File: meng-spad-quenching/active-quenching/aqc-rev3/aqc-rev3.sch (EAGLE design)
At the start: 252 parts, among them IC1 TPS7A4901, IC10 TPS7A3001, IC11 LT1534-1, IC12 74AHC1G04DBV, IC13 TLV271DBV, IC14 NC7WZ16P6X, IC15 LTC1711, IC16 HFA3134, IC17 HFA3135, IC18 USBLC6-2SC6Y, IC19 HFA3135, IC2 TPS7A4901, IC20 HFA3134, IC21 STM32F411RE, IC22 MAX572X, IC23 HFA3134, IC24 LM1117, IC25 HFA3134, IC26 THAT320, IC3 LT1534-1, IC4 TLV272DGK, IC5 ADCMP582, IC6 DS1100LU-20+, IC7 HFA3134, IC8 NC7SV74K8X, IC9 HFA3134, M1 BSS806N, M2 BSS806N, M3 BSS806N, Q6 IRLML6402TRPBF, SW1 MCU_RST, U1 MCP4725, U2 SN65EPT22DGK, U3 SN65EPT21DGK, X1 CONN_PULLDN_SENSE, X2 CONN_FORCE_QUENCH, X3 KEYSTONE-7774, X4 CONN_SPAD, X5 CONN_PHOTON_COUNTER, X6 KEYSTONE-7774, X7 CONN_SMU, X8 PN61729-S

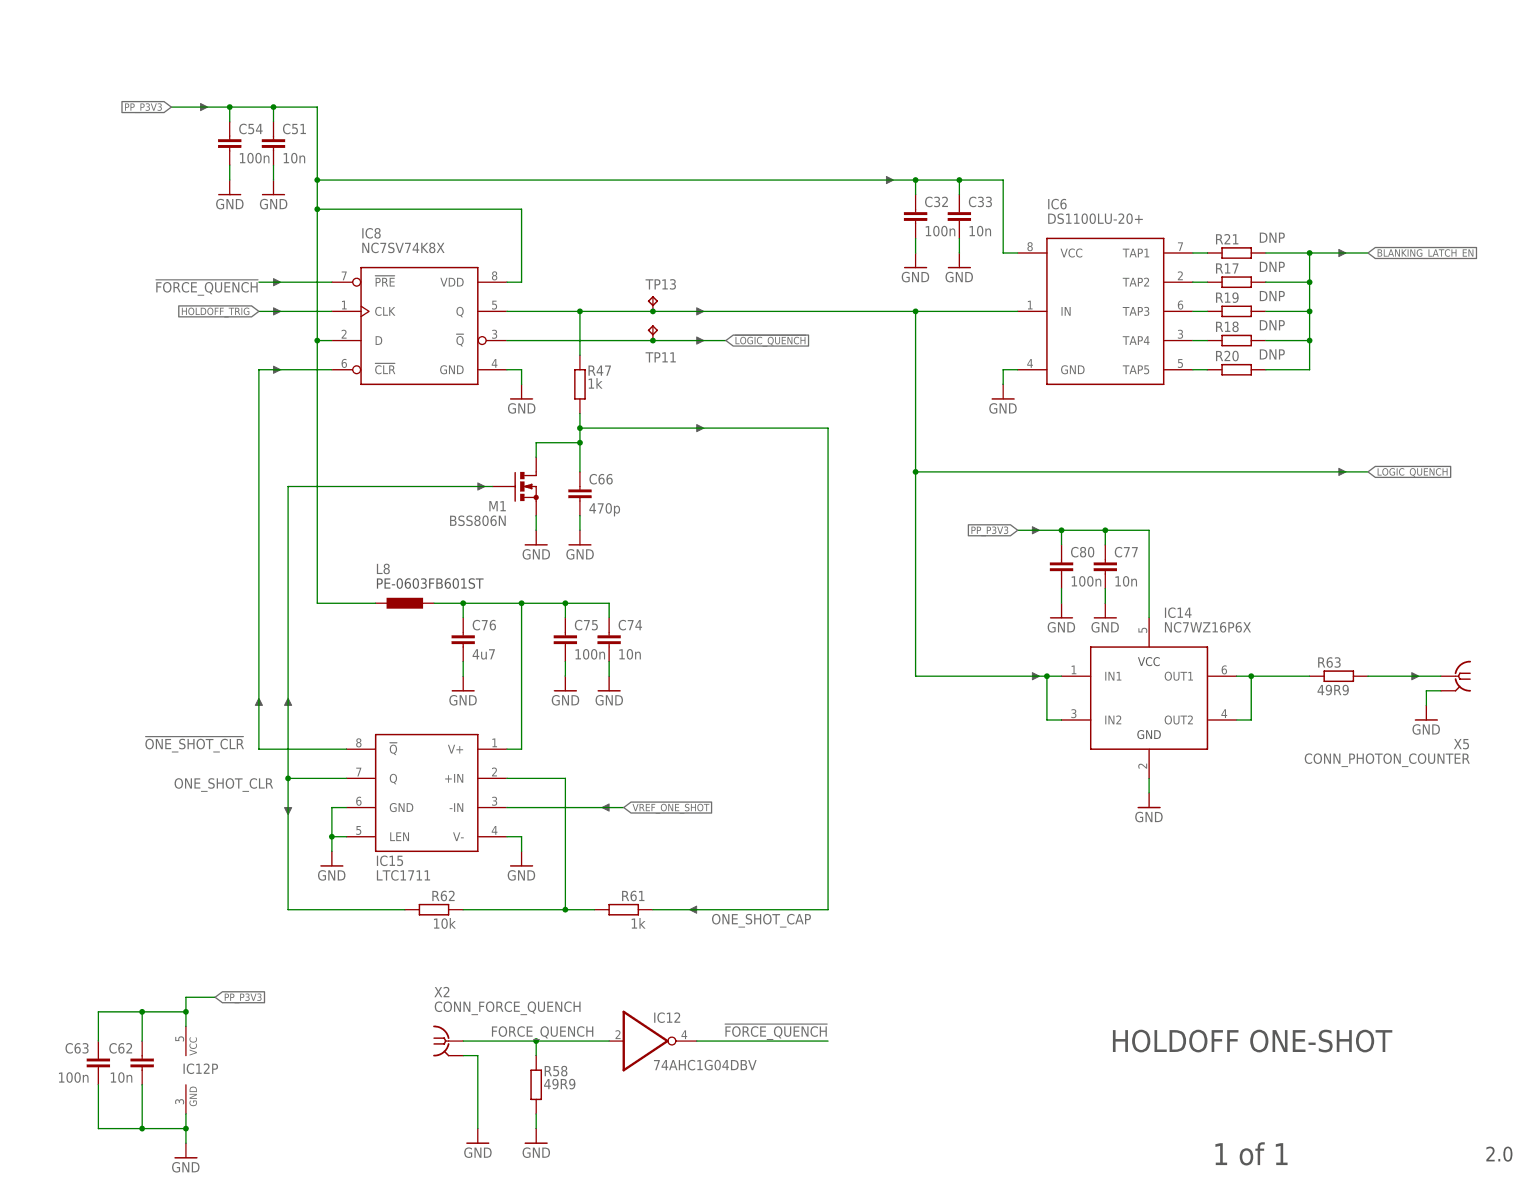
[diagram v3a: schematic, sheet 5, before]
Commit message: Improvements to one-shot and logic, more layout
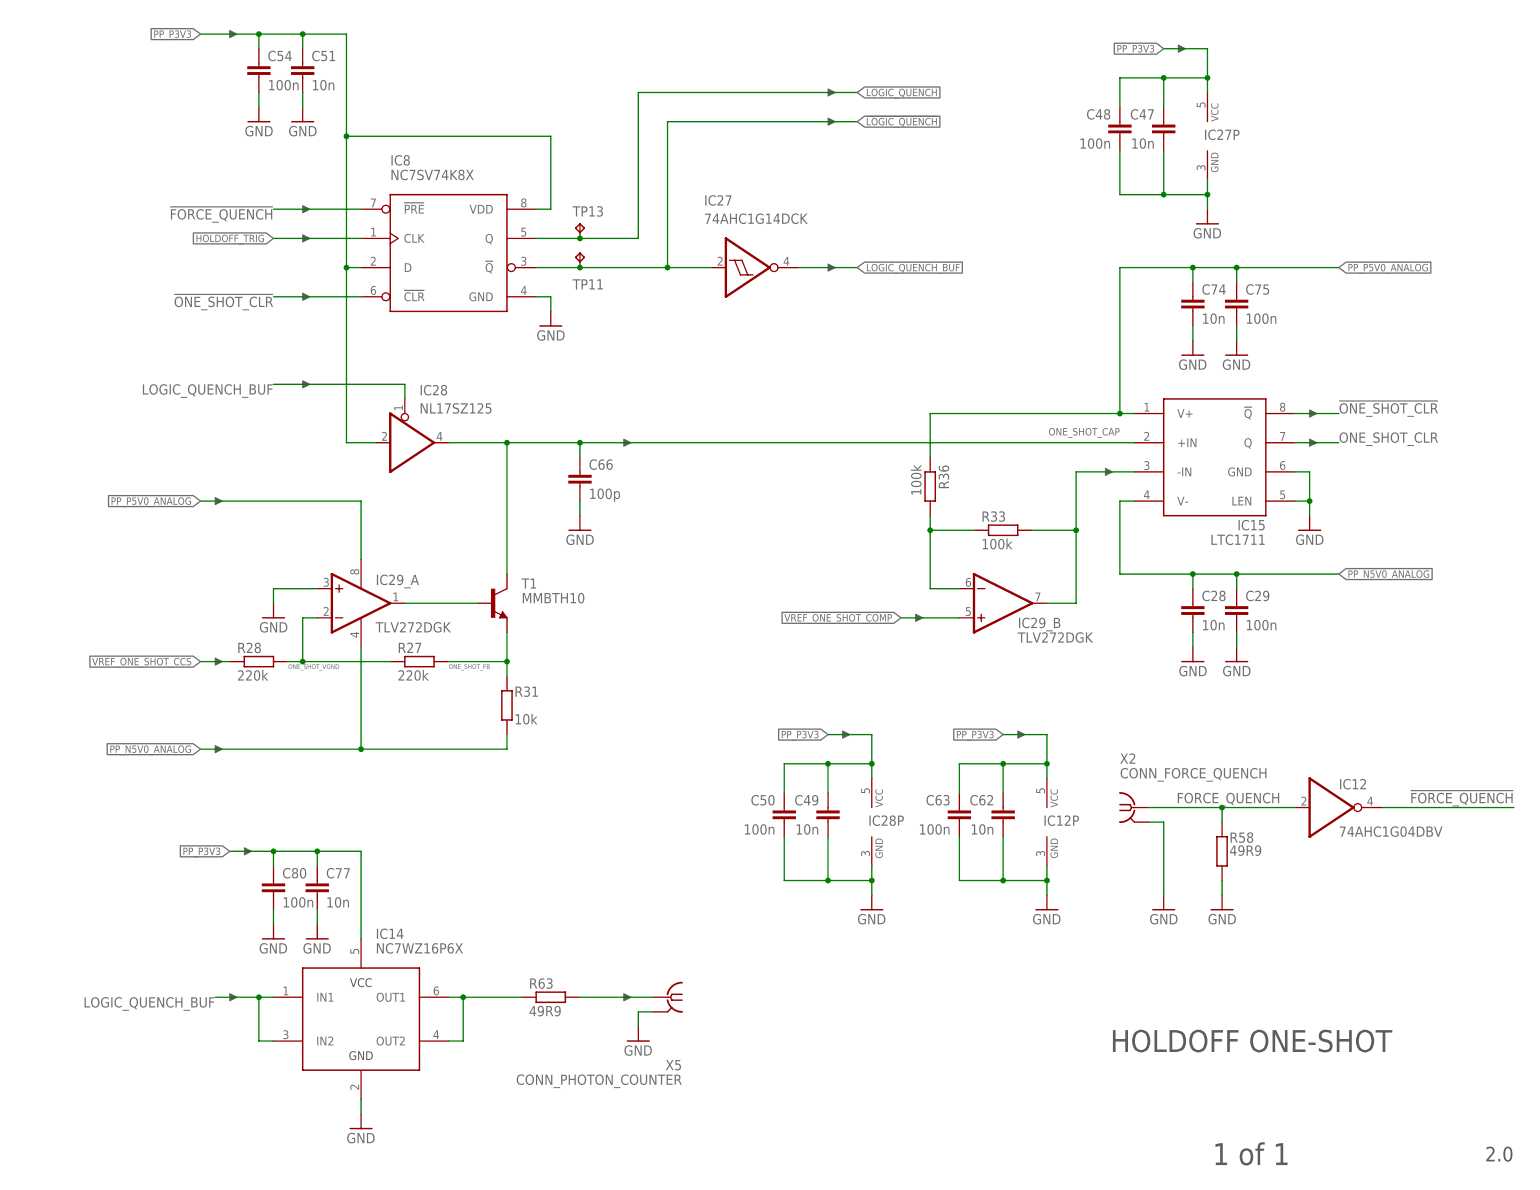
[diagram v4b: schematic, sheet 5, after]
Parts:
- removed C55: 100n, rcl-modified-footprints:C-EUC0603
- removed C76: 4u7, rcl:C-EUC0603
- removed L8: PE-0603FB601ST, meng:INDUCTOR0603
- removed M1: BSS806N, meng:BSS806N
- removed R47, R61: 1k, rcl:R-EU_R0603
- removed R62: 10k, rcl:R-EU_R0603
- added C19, C20, C28, C47, C49: 10n, rcl-modified-footprints:C-EUC0402
- added C29, C43, C48, C50: 100n, rcl-modified-footprints:C-EUC0402
- added IC27: 74AHC1G14DCK, 74xx-little-de:74AHC1G14DCK
- added IC28: NL17SZ125, 74xx-little-de:74AHC1G125DCK
- added IC29: TLV272DGK, meng:TLV272DGK
- added R27, R28: 220k, rcl-modified-footprints:R-EU_R0603
- added R31: 10k, rcl-modified-footprints:R-EU_R0603
- added R33, R36: 100k, rcl-modified-footprints:R-EU_R0603
- added R37, R42: DNP, rcl-modified-footprints:R-EU_R0603
- added T1: MMBTH10, transistor:MMBTH10LT1-NPN-SOT23-BEC
- C21: value 10n -> 100n
- C22, C27, C35, C42, C74, C75: device rcl:C-EUC0402 -> rcl-modified-footprints:C-EUC0402
- C36: value 1n -> 10n
- C37: value 100n -> 10n
- C66: value 470p -> 100p; device rcl:C-EUC0603 -> rcl-modified-footprints:C-EUC0603
- C95, C96: device rcl:C-EUC0603 -> rcl-modified-footprints:C-EUC0603
- R14: value 100R -> 1k
- R65: device rcl:R-EU_R0603 -> rcl-modified-footprints:R-EU_R0603
- R73, R81: value 100k -> 220k; device rcl:R-EU_R0603 -> rcl-modified-footprints:R-EU_R0603
- TP14: value CASC_IBIAS -> DELTA_V
- TP17: value SLEW_UP -> V_A
- TP18: value SLEW_DN -> EXTRA_1
- TP19: value SLEW_MAX -> EXTRA_2
- TP20: value (DELAY_UP) -> EXTRA_3
- TP21: value (DELAY_DN) -> EXTRA_4
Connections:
- net N$28 renamed PULLDN_SENSE_R_CONN
- removed net COMP_VP: C36.1, IC5.VP, R14.1
- removed net N$25: IC15.+IN, R61.1, R62.2
- removed net PP_P3V3_COMP: C74.1, C75.1, C76.1, IC15.V+, L8.P$2
- removed net PP_P3V3_DAC2: C17.1, C18.1, L2.P$2, U1.VDD
- removed net VREF_EXTRA_1: IC22.OUT4, TP18.P$1
- removed net VREF_ONE_SHOT: IC15.-IN, IC22.OUT2, TP16.P$1
- new net LOGIC_QUENCH_BUF: IC14.IN1, IC14.IN2, IC27A.O, IC28A.OE, IC6.IN
- new net N$1: R14.2, U1.VOUT
- new net N$10: IC29_B.-IN, R33.2, R36.1
- new net N$5: IC29_A.OUT, T1.B
- new net N$7: IC15.-IN, IC29_B.OUT, R33.1
- new net ONE_SHOT_FB: R27.1, R31.1, T1.E
- new net ONE_SHOT_VGND: IC29_A.-IN, R27.2, R28.1
- new net PP_P3V3_AV_DET_DAC: C17.1, C18.1, L2.P$2, R42.2, U1.VDD
- new net VREF_ONE_SHOT_CCS: IC22.OUT4, R28.2, TP18.P$1
- new net VREF_ONE_SHOT_COMP: IC22.OUT2, IC29_B.+IN, TP16.P$1
- net !LOGIC_QUENCH: now also IC27A.I
- net GND: now also C19.2, C20.2, C28.2, C29.2, C43.2, C47.2, C48.2, C49.2, C50.2, IC27P.GND, IC28P.GND, IC29_A.+IN, R37.1; no longer C55.2, C76.2, IC15.V-, M1.S
- net LOGIC_QUENCH: no longer IC14.IN1, IC14.IN2, IC6.IN, R47.2
- net ONE_SHOT_CAP: now also IC15.+IN, IC28A.O, T1.C; no longer M1.D, R47.1, R61.2
- net ONE_SHOT_CLR: no longer M1.G, R62.1
- net PP_N5V0_ANALOG: now also C28.1, C29.1, IC15.V-, IC29_A.V-, R31.2
- net PP_P15V0_ANALOG: no longer C55.1
- net PP_P3V3: now also C47.1, C48.1, C49.1, C50.1, IC27P.VCC, IC28A.I, IC28P.VCC; no longer L8.P$1
- net PP_P5V0_ANALOG: now also C19.1, C20.1, C74.1, C75.1, IC15.V+, IC29_A.V+, R36.2
- net VREF_AV_DET: now also C36.1, C43.1, IC5.VP, R14.1, R37.2, R42.1; no longer R14.2, U1.VOUT
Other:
- note added: "-IN"
- note added: "5V"
- note added: "Active-Low for Latch Mode (Note how Q0 goes to !LE!)"
- note added: "HIGH = Latch Enabled LOW = Latch Disabled"
- note added: "Insufficient recovery blanking results in self re-triggering Pick lowest delay tap that compensates a given coax cable"
- note added: "Note: comparator input pin has external capacitance connected, keep the driving pt. resistance high enough to ensure DAC opamp stability!"
- note added: "ONE_SHOT_CAP"
- note added: "Quenching can be forced at any time either by uC or from external input"
- note added: "Reduce loading of d-flop as much as possible for fast quenching"
- note added: "Reset holdoff timing cap when not quenching"
- note added: "This CCS BJT is always in FAR"
- note added: "avalanche detected"
- note added: "comp triggered"
- note added: "holdoff time"
- note removed: "4ns per tap, pick lowest tap that provides sufficient recovery blanking"
- note removed: "Active-Low for Latch Mode"
- note removed: "Assert before probe has landed"
- note removed: "From control logic"
- note removed: "HIGH = Latch Enabled"
- note removed: "LOW = Latch Disabled"
- note removed: "Note: insufficient recovery blanking = SPAD voltage oscillation"
- note removed: "Reduce loading of d-flop as much as possible"
- moved on the sheet: C21, C22, C23, C27, C34, C35, C36, C37, C38, C39, C42, C51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

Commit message: work on layout
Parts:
- added C55, C76: 10n, rcl:C-EUC0402
- added C64, C65, C73, C83: 100n, rcl:C-EUC0402
- added IC30: 74AHC1G32DCK, 74xx-little-de:74AHC1G32DCK
- added IC31: 74AHC1G08DCK, 74xx-little-de:74AHC1G08DCK
- added R44: 49R9, rcl:R-EU_R0603
- IC12: value 74AHC1G04DBV -> 74AHC1G04DCK; device 74xx-little-de:74AHC1G04DBV -> 74xx-little-de:74AHC1G04DCK
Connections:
- net ONE_SHOT_CLR renamed NC_ONE_SHOT_CLR
- removed net DAC1_CSB: IC21.PA15/JTDI, IC22.CSB
- new net DFLOP_!CLR: IC31A.O, IC8.!CLR
- new net FORCE_QUENCH_USER: IC30A.I0, R58.2, X2G1.1
- new net MCU_TIM2_CH1_IN: IC21.PA0, R44.1
- new net MCU_TIM2_CH1_OUT_1: IC21.PA5/SPI1_SCK, IC31A.I0
- new net MCU_TIM2_CH1_OUT_2: IC21.PA15/JTDI, IC30A.I1
- net !ONE_SHOT_CLR: now also IC31A.I1; no longer IC8.!CLR
- net FORCE_QUENCH: now also IC30A.O; no longer R58.2, X2G1.1
- net GND: now also C55.2, C64.2, C65.2, C73.2, C76.2, C83.2, IC22.CSB, IC30P.GND, IC31P.GND
- net LOGIC_QUENCH_BUF: now also R44.2
- net PP_N5V0_ANALOG: now also C73.1
- net PP_P3V3: now also C55.1, C64.1, C76.1, C83.1, IC30P.VCC, IC31P.VCC
- net PP_P5V0_ANALOG: now also C65.1
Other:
- note added: ""chip_select_bar" always asserted"
- note added: "AND"
- note added: "OR"
- note added: "Pulling either input low will assert !CLR! on d-flop"
- note removed: "12"
- note removed: "CS"
- note removed: "OPTIONAL SLEW GENERATOR"
- note removed: "Panasonic EEF-CX1D470R"
- moved on the sheet: C28, C29, C47, C48, C49, C50, C51, C54, C62, C63, C66, C74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

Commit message: work on layout
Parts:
- removed C102: 100n, rcl:C-EUC0603
- added R45: 0R, resistor:R-EU_R0603
- C76, C83: device rcl:C-EUC0402 -> rcl-modified-footprints:C-EUC0402
- R44: device rcl:R-EU_R0603 -> rcl-modified-footprints:R-EU_R0603
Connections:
- net GND: now also R45.2; no longer C102.2
- net MCU_VCAP_1: now also R45.1; no longer C102.1
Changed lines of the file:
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@@
 <part name="C109" library="rcl" deviceset="C-EU" device="C0603" value="100n"/>
 <part name="GND80" library="SparkFun-Aesthetics" deviceset="GND" device=""/>
-<part name="C102" library="rcl" deviceset="C-EU" device="C0603" value="100n"/>
 <part name="C100" library="rcl" deviceset="C-EU" device="C0603" value="100n"/>
 <part name="GND81" library="SparkFun-Aesthetics" deviceset="GND" device=""/>
@@
 <part name="DNP90" library="meng" deviceset="ARROW_1DIR" device=""/>
 <part name="DNP91" library="meng" deviceset="ARROW_1DIR" device=""/>
-<part name="R44" library="rcl" deviceset="R-EU_" device="R0603" value="49R9"/>
+<part name="R44" library="rcl-modified-footprints" deviceset="R-EU_" device="R0603" package3d_urn="urn:adsk.eagle:package:23555/2" value="49R9"/>
 <part name="DNP45" library="meng" deviceset="ARROW_1DIR" device=""/>
 <part name="IC31" library="74xx-little-de" library_urn="urn:adsk.eagle:library:86" deviceset="74*1G08" device="DCK" package3d_urn="urn:adsk.eagle:package:2405/1" technology="AHC"/>
 <part name="DNP112" library="meng" deviceset="ARROW_1DIR" device=""/>
 <part name="DNP113" library="meng" deviceset="ARROW_1DIR" device=""/>
-<part name="C76" library="rcl" deviceset="C-EU" device="C0402" value="10n"/>
-<part name="C83" library="rcl" deviceset="C-EU" device="C0402" value="100n"/>
+<part name="C76" library="rcl-modified-footprints" deviceset="C-EU" device="C0402" package3d_urn="urn:adsk.eagle:package:23626/1" value="10n"/>
+<part name="C83" library="rcl-modified-footprints" deviceset="C-EU" device="C0402" package3d_urn="urn:adsk.eagle:package:23626/1" value="100n"/>
 <part name="GND93" library="supply1" deviceset="GND" device=""/>
 <part name="DNP114" library="meng" deviceset="ARROW_1DIR" device=""/>
+<part name="R45" library="resistor" deviceset="R-EU_" device="R0603" value="0R"/>
 </parts>
 <sheets>
@@
 </instance>
 <instance part="GND80" gate="1" x="213.36" y="104.14"/>
-<instance part="C102" gate="G$1" x="66.04" y="78.74" smashed="yes">
-<attribute name="NAME" x="67.564" y="79.121" size="1.778" layer="95"/>
-<attribute name="VALUE" x="67.564" y="74.041" size="1.778" layer="96"/>
-</instance>
 <instance part="C100" gate="G$1" x="55.88" y="78.74" smashed="yes">
 <attribute name="NAME" x="57.404" y="79.121" size="1.778" layer="95"/>
 <attribute name="VALUE" x="57.404" y="74.041" size="1.778" layer="96"/>
 </instance>
-<instance part="GND81" gate="1" x="66.04" y="68.58"/>
-<instance part="GND90" gate="1" x="55.88" y="68.58"/>
+<instance part="GND81" gate="1" x="66.04" y="66.04"/>
+<instance part="GND90" gate="1" x="55.88" y="66.04"/>
 <instance part="DNP73" gate="G$1" x="175.26" y="127"/>
 <instance part="DNP92" gate="G$1" x="175.26" y="129.54"/>
@@
 <instance part="DNP90" gate="G$1" x="106.68" y="129.54"/>
 <instance part="DNP91" gate="G$1" x="106.68" y="111.76" rot="R180"/>
+<instance part="R45" gate="G$1" x="66.04" y="76.2" smashed="yes" rot="MR270">
+<attribute name="NAME" x="67.31" y="79.7814" size="1.778" layer="95" rot="MR180"/>
+<attribute name="VALUE" x="67.31" y="74.422" size="1.778" layer="96" rot="MR180"/>
+</instance>
 </instances>
 <busses>
@@
 <pinref part="GND90" gate="1" pin="GND"/>
 <pinref part="C100" gate="G$1" pin="2"/>
-<wire x1="55.88" y1="71.12" x2="55.88" y2="73.66" width="0.1524" layer="91"/>
+<wire x1="55.88" y1="68.58" x2="55.88" y2="73.66" width="0.1524" layer="91"/>
 </segment>
 <segment>
 <pinref part="GND81" gate="1" pin="GND"/>
-<pinref part="C102" gate="G$1" pin="2"/>
-<wire x1="66.04" y1="71.12" x2="66.04" y2="73.66" width="0.1524" layer="91"/>
+<wire x1="66.04" y1="68.58" x2="66.04" y2="71.12" width="0.1524" layer="91"/>
+<pinref part="R45" gate="G$1" pin="2"/>
 </segment>
 <segment>
@@
 <segment>
 <pinref part="IC21" gate="G$1" pin="VCAP_1"/>
-<pinref part="C102" gate="G$1" pin="1"/>
 <wire x1="111.76" y1="86.36" x2="66.04" y2="86.36" width="0.1524" layer="91"/>
 <wire x1="66.04" y1="86.36" x2="66.04" y2="81.28" width="0.1524" layer="91"/>
 <label x="83.82" y="83.82" size="1.778" layer="95" rot="MR0"/>
+<pinref part="R45" gate="G$1" pin="1"/>
 </segment>
 </net>

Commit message: First-pass layout complete
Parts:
- C100, C107, C91, C92: device rcl:C-EUC0603 -> rcl-modified-footprints:C-EUC0603
- C65, C73: device rcl:C-EUC0402 -> rcl-modified-footprints:C-EUC0402
- R45, R74, R75, R78, R79: device resistor:R-EU_R0603 -> rcl-modified-footprints:R-EU_R0603
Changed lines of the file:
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@@
 <part name="DNP58" library="meng" deviceset="ARROW_1DIR" device=""/>
 <part name="C84" library="rcl" deviceset="C-EU" device="C0603" value="100n"/>
-<part name="C91" library="rcl" deviceset="C-EU" device="C0603" value="100n"/>
-<part name="C92" library="rcl" deviceset="C-EU" device="C0603" value="100n"/>
+<part name="C91" library="rcl-modified-footprints" deviceset="C-EU" device="C0603" package3d_urn="urn:adsk.eagle:package:23616/2" value="100n"/>
+<part name="C92" library="rcl-modified-footprints" deviceset="C-EU" device="C0603" package3d_urn="urn:adsk.eagle:package:23616/2" value="100n"/>
 <part name="C81" library="rcl" deviceset="C-EU" device="C0603" value="4u7"/>
 <part name="GND33" library="supply1" deviceset="GND" device=""/>
@@
 <part name="C109" library="rcl" deviceset="C-EU" device="C0603" value="100n"/>
 <part name="GND80" library="SparkFun-Aesthetics" deviceset="GND" device=""/>
-<part name="C100" library="rcl" deviceset="C-EU" device="C0603" value="100n"/>
+<part name="C100" library="rcl-modified-footprints" deviceset="C-EU" device="C0603" package3d_urn="urn:adsk.eagle:package:23616/2" value="100n"/>
 <part name="GND81" library="SparkFun-Aesthetics" deviceset="GND" device=""/>
 <part name="GND90" library="SparkFun-Aesthetics" deviceset="GND" device=""/>
@@
 <part name="GND109" library="supply1" deviceset="GND" device=""/>
 <part name="GND110" library="supply1" deviceset="GND" device=""/>
-<part name="R79" library="resistor" deviceset="R-EU_" device="R0603" value="DNP"/>
-<part name="R75" library="resistor" deviceset="R-EU_" device="R0603" value="DNP"/>
+<part name="R79" library="rcl-modified-footprints" deviceset="R-EU_" device="R0603" package3d_urn="urn:adsk.eagle:package:23555/2" value="DNP"/>
+<part name="R75" library="rcl-modified-footprints" deviceset="R-EU_" device="R0603" package3d_urn="urn:adsk.eagle:package:23555/2" value="DNP"/>
 <part name="GND111" library="supply1" deviceset="GND" device=""/>
 <part name="DNP129" library="meng" deviceset="ARROW_1DIR" device=""/>
 <part name="DNP130" library="meng" deviceset="ARROW_1DIR" device=""/>
-<part name="R78" library="resistor" deviceset="R-EU_" device="R0603" value="0R"/>
-<part name="R74" library="resistor" deviceset="R-EU_" device="R0603" value="DNP"/>
+<part name="R78" library="rcl-modified-footprints" deviceset="R-EU_" device="R0603" package3d_urn="urn:adsk.eagle:package:23555/2" value="0R"/>
+<part name="R74" library="rcl-modified-footprints" deviceset="R-EU_" device="R0603" package3d_urn="urn:adsk.eagle:package:23555/2" value="DNP"/>
 <part name="GND117" library="supply1" deviceset="GND" device=""/>
 <part name="DNP131" library="meng" deviceset="ARROW_1DIR" device=""/>
@@
 <part name="GND160" library="supply1" deviceset="GND" device=""/>
 <part name="DNP10" library="meng" deviceset="ARROW_1DIR" device=""/>
-<part name="C107" library="rcl" deviceset="C-EU" device="C0603" value="100n"/>
+<part name="C107" library="rcl-modified-footprints" deviceset="C-EU" device="C0603" package3d_urn="urn:adsk.eagle:package:23616/2" value="100n"/>
 <part name="GND156" library="supply1" deviceset="GND" device=""/>
 <part name="RLY1" library="meng" deviceset="MEDER_CRF05-1A" device="" value="CRF05-1A"/>
@@
 <part name="DNP86" library="meng" deviceset="ARROW_1DIR" device=""/>
 <part name="DNP87" library="meng" deviceset="ARROW_1DIR" device=""/>
-<part name="C65" library="rcl" deviceset="C-EU" device="C0402" value="100n"/>
-<part name="C73" library="rcl" deviceset="C-EU" device="C0402" value="100n"/>
+<part name="C65" library="rcl-modified-footprints" deviceset="C-EU" device="C0402" package3d_urn="urn:adsk.eagle:package:23626/1" value="100n"/>
+<part name="C73" library="rcl-modified-footprints" deviceset="C-EU" device="C0402" package3d_urn="urn:adsk.eagle:package:23626/1" value="100n"/>
 <part name="GND92" library="supply1" deviceset="GND" device=""/>
 <part name="DNP88" library="meng" deviceset="ARROW_1DIR" device=""/>
@@
 <part name="GND93" library="supply1" deviceset="GND" device=""/>
 <part name="DNP114" library="meng" deviceset="ARROW_1DIR" device=""/>
-<part name="R45" library="resistor" deviceset="R-EU_" device="R0603" value="0R"/>
+<part name="R45" library="rcl-modified-footprints" deviceset="R-EU_" device="R0603" package3d_urn="urn:adsk.eagle:package:23555/2" value="0R"/>
 </parts>
 <sheets>
